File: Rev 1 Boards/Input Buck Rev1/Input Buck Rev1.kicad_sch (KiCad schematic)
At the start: 0 parts

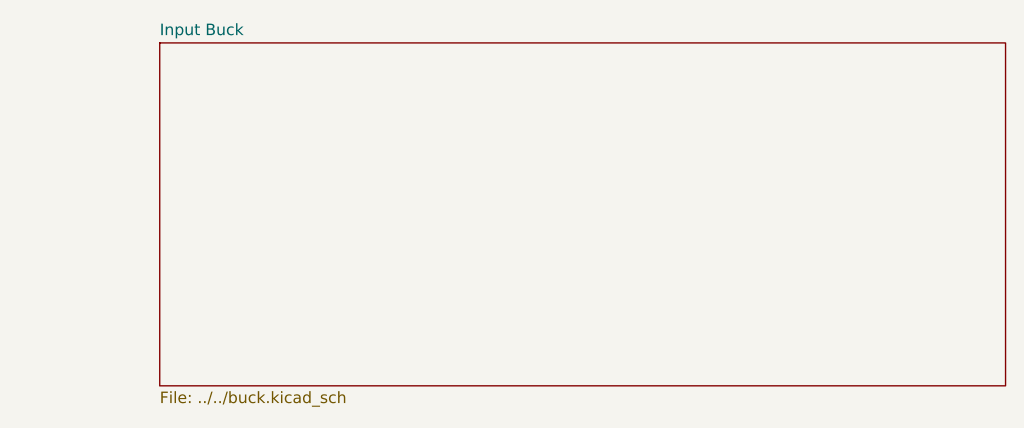
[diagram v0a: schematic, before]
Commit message: Added tps, connectors for Input Buck
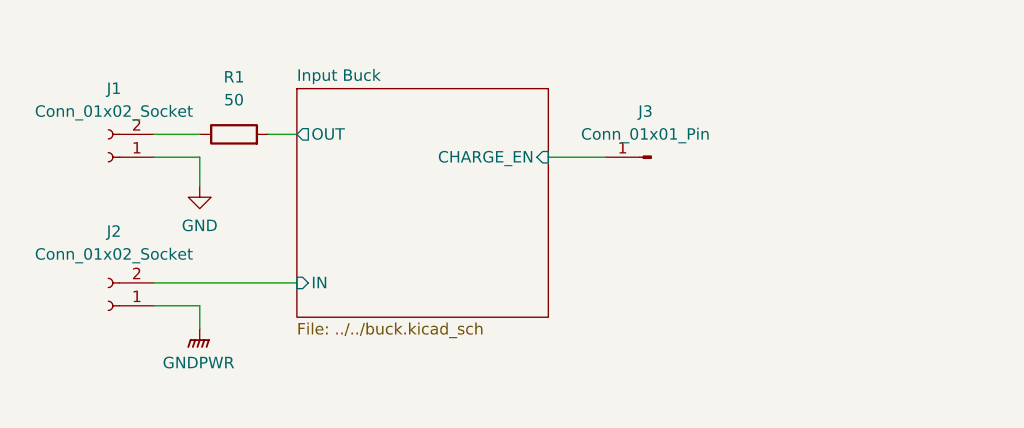
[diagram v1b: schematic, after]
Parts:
- added J1, J2: Conn_01x02_Socket, symbol Connector:Conn_01x02_Socket
- added J3: Conn_01x01_Pin, symbol Connector:Conn_01x01_Pin
- added R1: 50, symbol Device:R
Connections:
- new net: J1.2 (Pin_2), R1.1
- new net GND: J1.1 (Pin_1)
- new net GNDPWR: J2.1 (Pin_1)
- new net Input Buck/CHARGE_EN: J3.1 (Pin_1)
- new net Input Buck/IN: J2.2 (Pin_2)
- new net Input Buck/OUT: R1.2
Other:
- sheet Input Buck ports: added CHARGE_EN, IN, OUT; removed none

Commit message: Layout iteration 1 for the input buck
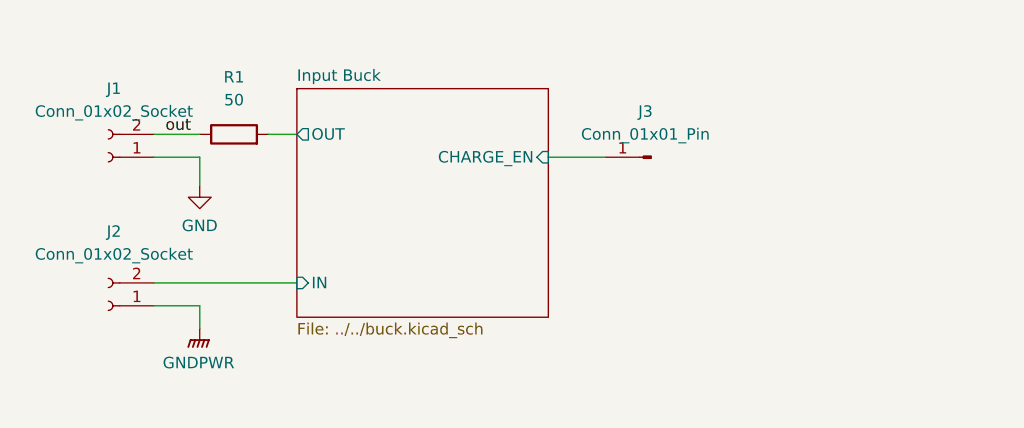
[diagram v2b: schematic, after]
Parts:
- J1, J2: footprint (none) -> Connector:Banana_Jack_2Pin
- J3: footprint (none) -> Connector_PinHeader_2.54mm:PinHeader_1x01_P2.54mm_Vertical
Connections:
- net out: now reaches J1.2 (Pin_2), R1.1
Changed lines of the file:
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@@
+		)
+	)
+	(label "out"
+		(at 50.165 93.98 0)
+		(effects
+			(font
+				(size 1.27 1.27)
+			)
+			(justify left bottom)
 		)
 	)
@@
 			)
 		)
-		(property "Footprint" ""
+		(property "Footprint" "Connector:Banana_Jack_2Pin"
 			(at 43.815 113.03 0)
 			(effects
@@
 		)
 		(property "Description" "Generic connector, single row, 01x02, script generated"
+			(at 43.815 113.03 0)
+			(effects
+				(font
+					(size 1.27 1.27)
+				)
+				(hide yes)
+			)
+		)
+		(property "Mouser #" ""
+			(at 43.815 113.03 0)
+			(effects
+				(font
+					(size 1.27 1.27)
+				)
+				(hide yes)
+			)
+		)
+		(property "Mouser Link" ""
+			(at 43.815 113.03 0)
+			(effects
+				(font
+					(size 1.27 1.27)
+				)
+				(hide yes)
+			)
+		)
+		(property "JLCPCB #" ""
 			(at 43.815 113.03 0)
 			(effects
@@
 			)
 		)
-		(property "Footprint" ""
+		(property "Footprint" "Connector_PinHeader_2.54mm:PinHeader_1x01_P2.54mm_Vertical"
 			(at 104.14 96.52 0)
 			(effects
@@
 		)
 		(property "Description" "Generic connector, single row, 01x01, script generated"
+			(at 104.14 96.52 0)
+			(effects
+				(font
+					(size 1.27 1.27)
+				)
+				(hide yes)
+			)
+		)
+		(property "Mouser #" ""
+			(at 104.14 96.52 0)
+			(effects
+				(font
+					(size 1.27 1.27)
+				)
+				(hide yes)
+			)
+		)
+		(property "Mouser Link" ""
+			(at 104.14 96.52 0)
+			(effects
+				(font
+					(size 1.27 1.27)
+				)
+				(hide yes)
+			)
+		)
+		(property "JLCPCB #" ""
 			(at 104.14 96.52 0)
 			(effects
@@
 			)
 		)
-		(property "Footprint" ""
+		(property "Footprint" "Connector:Banana_Jack_2Pin"
 			(at 43.815 96.52 0)
 			(effects
@@
 			(at 43.815 96.52 0)
 			(effects
+				(font
+					(size 1.27 1.27)
+				)
+				(hide yes)
+			)
+		)
+		(property "Mouser #" ""
+			(at 43.815 96.52 0)
+			(effects
+				(font
+					(size 1.27 1.27)
+				)
+				(hide yes)
+			)
+		)
+		(property "Mouser Link" ""
+			(at 43.815 96.52 0)
+			(effects
+				(font
+					(size 1.27 1.27)
+				)
+				(hide yes)
+			)
+		)
+		(property "JLCPCB #" ""
+			(at 43.815 96.52 0)
+			(effects

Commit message: Minor changes
Still need to replace the inductor footprint with the correct one
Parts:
- R1: footprint (none) -> Resistor_SMD:R_0603_1608Metric_Pad0.98x0.95mm_HandSolder
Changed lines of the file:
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@@
 			)
 		)
-		(property "Footprint" ""
+		(property "Footprint" "Resistor_SMD:R_0603_1608Metric_Pad0.98x0.95mm_HandSolder"
 			(at 57.785 95.758 90)
 			(effects
@@
 			(at 57.785 93.98 0)
 			(effects
+				(font
+					(size 1.27 1.27)
+				)
+				(hide yes)
+			)
+		)
+		(property "Mouser #" ""
+			(at 57.785 93.98 0)
+			(effects
+				(font
+					(size 1.27 1.27)
+				)
+				(hide yes)
+			)
+		)
+		(property "Mouser Link" ""
+			(at 57.785 93.98 0)
+			(effects
+				(font
+					(size 1.27 1.27)
+				)
+				(hide yes)
+			)
+		)
+		(property "JLCPCB #" ""
+			(at 57.785 93.98 0)
+			(effects
